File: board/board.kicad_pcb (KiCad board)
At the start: 2 copper layers, 165 x 54 mm, 27 parts, among them J1 Conn_01x01_Female, J2 Conn_01x01_Female, J3 Conn_01x01_Female, J4 Conn_01x01_Female, J5 Conn_02x14_Odd_Even, J6 Conn_02x12_Odd_Even, J7 Conn_01x01_Female, J8 Conn_01x01_Female, J9 Conn_01x01_Female, SW1 reset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

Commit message: Memory routed.
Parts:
- R3: moved to B.Cu
- moved J5 128.1 mm to (307.2, 50.0)
- moved U2 99.4 mm to (226.1, 86.4)
- moved U3 95.2 mm to (226.0, 53.3)
- moved C3 86.5 mm to (226.7, 29.8)
- moved C2 81.3 mm to (232.2, 30.5)
- moved J2 5.20 mm to (170.2, 45.7)
- moved J9 4.94 mm to (73.7, 82.4)
- moved R3 4.44 mm to (140.7, 43.8), turned to 180 degrees
- moved J1 3.97 mm to (170.2, 39.5)
- moved J3 3.37 mm to (163.7, 45.7)
- moved C0 2.72 mm to (146.5, 40.1)
- moved SW1 2.72 mm to (155.8, 39.0)
- moved J8 2.40 mm to (68.6, 82.4)
- moved J4 0.31 mm to (163.7, 39.5)
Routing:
- net /#RES: track 73.2 -> 170.2 mm, vias 2 -> 1
- net /GND: track 51.1 -> 78.7 mm
- net /a11: track 3.05 -> 28.5 mm
- net /a10: track 6.69 -> 26.7 mm
- net /#CE: track 0.00 -> 17.2 mm
- net /d7: track 26.3 -> 40.9 mm
- net /d6: track 29.7 -> 41.5 mm
- net /d5: track 35.4 -> 44.4 mm
- net /d4: track 35.7 -> 42.0 mm
- net /d3: track 57.6 -> 61.3 mm
- net /a2: track 99.7 -> 98.8 mm
- net /a1: track 100.5 -> 99.6 mm
- net /a0: track 103.3 -> 102.4 mm
- net /a3: track 101.0 -> 100.1 mm

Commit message: Corrected AND gate schematics + start on control.
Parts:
- C2, C3, C4, C5: moved to B.Cu
- U5: value 74LS08 -> 2-AND
- moved U3 130.4 mm to (95.6, 55.8)
- moved C3 112.5 mm to (117.8, 57.9)
- moved U2 97.3 mm to (133.7, 55.8)
- moved J5 93.6 mm to (221.0, 86.4), turned to 180 degrees
- moved C2 82.1 mm to (154.8, 57.9)
- moved R3 37.7 mm to (141.1, 81.5)
- moved SW1 37.7 mm to (156.2, 76.7)
- moved C0 37.7 mm to (146.9, 77.8)
- moved J1 37.7 mm to (170.6, 77.2)
- moved J2 37.7 mm to (170.6, 83.4)
- moved J3 37.7 mm to (164.1, 83.4)
- moved J4 37.7 mm to (164.1, 77.2)
- moved C5 10.5 mm to (111.0, 81.1), turned to 270 degrees
- moved C4 10.2 mm to (103.5, 81.7), turned to 270 degrees
- moved U4 9.96 mm to (103.4, 81.5)
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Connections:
- U3 pad 20: Net-(U3-Pad20) -> /#RAM_E
- U4 pad 14: (no net) -> /+5V
- U4 pad 6: Net-(U4-Pad6) -> /NAND1
- U4 pad 7: (no net) -> /GND
- U5 pad 1: /#DMA -> /NAND1
- U5 pad 2: Net-(U4-Pad6) -> /#DMA
- U5 pad 3: Net-(U3-Pad20) -> /GND
- U5 pad 4: (no net) -> /#RAM_E
- U5 pad 5: (no net) -> /+5V
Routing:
- net /a14: track 0.00 -> 105.6 mm, vias 0 -> 2
- net /+5V: track 55.3 -> 150.8 mm, vias 4 -> 6
- net /a12: track 6.69 -> 96.1 mm, vias 0 -> 2
- net /a7: track 3.05 -> 90.9 mm, vias 0 -> 2
- net /a6: track 3.05 -> 89.4 mm, vias 0 -> 2
- net /a13: track 49.1 -> 135.5 mm, vias 0 -> 2
- net /a8: track 6.69 -> 91.5 mm, vias 0 -> 2
- net /a5: track 6.69 -> 91.5 mm, vias 0 -> 2
- net /a9: track 3.05 -> 86.4 mm, vias 0 -> 2
- net /a4: track 3.05 -> 86.4 mm, vias 0 -> 2
- net /a3: track 100.1 -> 181.9 mm, vias 0 -> 2
- net /#RES: track 170.2 -> 89.8 mm
- net /d0: track 49.4 -> 129.7 mm, vias 4 -> 6
- net /a2: track 98.8 -> 179.0 mm, vias 1 -> 3
- net /a1: track 99.6 -> 178.4 mm, vias 0 -> 2
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
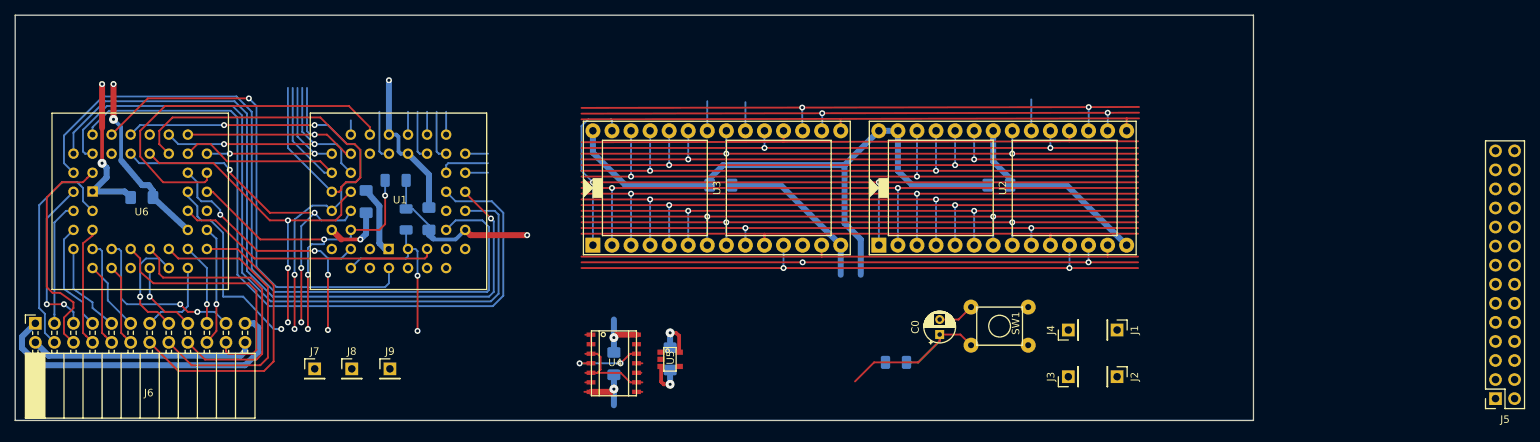
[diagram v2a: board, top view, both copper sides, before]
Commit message: Adress + data I/O routed.
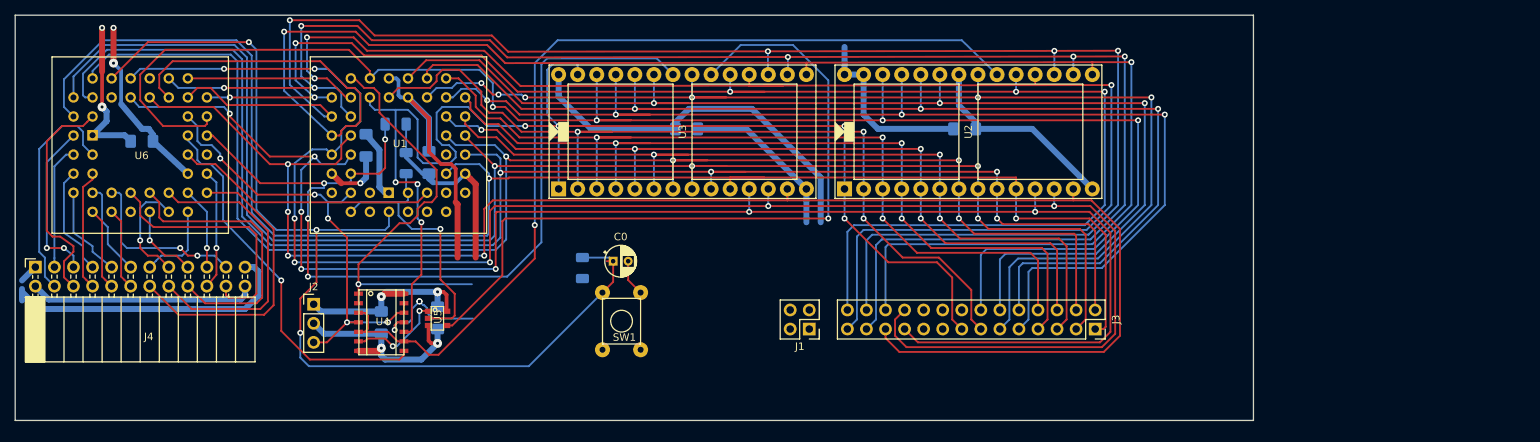
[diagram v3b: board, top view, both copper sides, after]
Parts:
- removed J5: Conn_02x14_Odd_Even, Connector_PinSocket_2.54mm:PinSocket_2x14_P2.54mm_Vertical
- removed J6: Conn_02x12_Odd_Even, Connector_PinSocket_2.54mm:PinSocket_2x12_P2.54mm_Horizontal
- removed J7, J8, J9: Conn_01x01_Female, Connector_PinHeader_2.54mm:PinHeader_1x01_P2.54mm_Vertical
- J1: value Conn_01x01_Female -> Conn_01x04_Male; footprint Connector_PinHeader_2.54mm:PinHeader_1x01_P2.54mm_Vertical -> Connector_PinHeader_2.54mm:PinHeader_2x02_P2.54mm_Vertical
- J2: value Conn_01x01_Female -> Conn_01x03_Male; footprint Connector_PinHeader_2.54mm:PinHeader_1x01_P2.54mm_Vertical -> Connector_PinHeader_2.54mm:PinHeader_1x03_P2.54mm_Vertical
- J3: value Conn_01x01_Female -> Conn_02x14_Odd_Even; footprint Connector_PinHeader_2.54mm:PinHeader_1x01_P2.54mm_Vertical -> Connector_PinSocket_2.54mm:PinSocket_2x14_P2.54mm_Vertical
- J4: value Conn_01x01_Female -> Conn_02x12_Odd_Even; footprint Connector_PinHeader_2.54mm:PinHeader_1x01_P2.54mm_Vertical -> Connector_PinSocket_2.54mm:PinSocket_2x12_P2.54mm_Horizontal
- moved J4 137.9 mm to (26.4, 68.8)
- moved J2 107.5 mm to (63.5, 73.8), turned to 0 degrees
- moved SW1 51.7 mm to (104.5, 77.3), turned to 0 degrees
- moved C0 44.6 mm to (103.4, 68.0), turned to 0 degrees
- moved R3 43.6 mm to (99.3, 69.0), turned to 270 degrees
- moved J1 41.0 mm to (129.5, 77.1), turned to 180 degrees
- moved C4 31.5 mm to (72.5, 76.2)
- moved C5 31.5 mm to (80.0, 75.6)
- moved U4 31.5 mm to (72.4, 76.1)
- moved U5 31.5 mm to (80.8, 75.6)
- moved C3 8.78 mm to (113.2, 50.4)
- moved U2 8.78 mm to (129.2, 48.3)
- moved U3 8.78 mm to (91.1, 48.3)
- moved C2 8.78 mm to (150.2, 50.4)
- moved U1 7.49 mm to (73.5, 58.9)
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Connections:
- J2 pad 1: /MASTER_GND -> /+5V
- J3 pad 1: /+5V -> /a0
- J4 pad 1: /GND -> /MASTER_VCC
- U4 pad 14: /+5V -> (no net)
- U4 pad 7: /GND -> (no net)
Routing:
- net /#CE: track 16.8 -> 124.6 mm, vias 0 -> 1
- net /d4: track 114.7 -> 219.7 mm, vias 4 -> 6
- net /d5: track 115.9 -> 220.9 mm, vias 2 -> 4
- net /d6: track 106.8 -> 210.5 mm, vias 1 -> 3
- net /d3: track 135.2 -> 238.4 mm, vias 0 -> 2
- net /d7: track 105.1 -> 205.9 mm, vias 4 -> 6
- net /#RAM_E: track 3.81 -> 98.6 mm, vias 0 -> 1
- net /d1: track 141.7 -> 234.6 mm, vias 6 -> 7
- net /d2: track 123.9 -> 215.8 mm, vias 3 -> 4
- net /d0: track 129.7 -> 214.4 mm, vias 6 -> 7
- net /a13: track 135.5 -> 215.7 mm, vias 2 -> 4
- net /a14: track 105.6 -> 180.5 mm, vias 2 -> 7
- net /#RW: track 51.3 -> 123.4 mm
- net /a11: track 84.8 -> 156.4 mm, vias 2 -> 3
- net /a9: track 86.4 -> 155.4 mm, vias 2 -> 3
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
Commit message: All connections done.
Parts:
- moved C3 5.80 mm to (118.5, 52.7)
- moved C6 5.80 mm to (45.9, 54.4)
- moved C7 5.80 mm to (75.8, 54.9)
- moved J1 5.80 mm to (134.9, 79.4)
- moved J3 5.80 mm to (173.0, 79.4)
- moved R1 5.80 mm to (81.2, 57.3)
- moved R2 5.80 mm to (79.8, 52.1)
- moved R3 5.80 mm to (104.6, 71.2)
- moved SW1 5.80 mm to (109.9, 79.6)
- moved U1 5.80 mm to (78.9, 61.2)
- moved U2 5.80 mm to (134.5, 50.5)
- moved U3 5.80 mm to (96.4, 50.5)
- moved J4 5.80 mm to (31.8, 71.1)
- moved C0 5.80 mm to (108.7, 70.3)
- moved C4 5.80 mm to (77.9, 78.5)
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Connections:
- U4 pad 14: (no net) -> /+5V
- U4 pad 7: (no net) -> /GND
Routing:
- net /MASTER_GND: track 30.1 -> 149.7 mm, vias 0 -> 1
- net /MASTER_VCC: track 42.5 -> 143.3 mm
- net /#CLK: track 16.5 -> 89.8 mm, vias 3 -> 7
- net /#DMA: track 36.0 -> 106.2 mm, vias 1 -> 4
- net /a15: track 56.5 -> 125.7 mm, vias 1 -> 3
- net /GND: track 152.5 -> 194.7 mm, vias 4 -> 10
- net /a14: track 180.5 -> 186.0 mm
- net /+5V: track 161.7 -> 158.5 mm, vias 5 -> 16
- net /a12: track 117.8 -> 120.1 mm
- net /#RES: track 136.6 -> 135.7 mm
- net /#CE: track 124.6 -> 125.3 mm
- net /#RW: track 123.4 -> 122.7 mm
- added copper zone on F.Cu, net /+5V
- added copper zone on B.Cu, net /GND
